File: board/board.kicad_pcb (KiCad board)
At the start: 4 copper layers, 21 x 77 mm, 72 parts, among them J1 UART, J2 008_USB, J3 DebugEdge_02x05, J4 019_100BASE-T_with_CT, J5 ADC_2x3, J6 SWD_6_Pol_Needle, J7 SPI_2x3, J8 I2C_2x2, J9 UART_2x2, U1 W25Q128JVS, U2 RP2040, U3 W5500, U4 11AA02E48, Y1 12MhZ, Y2 25MHz

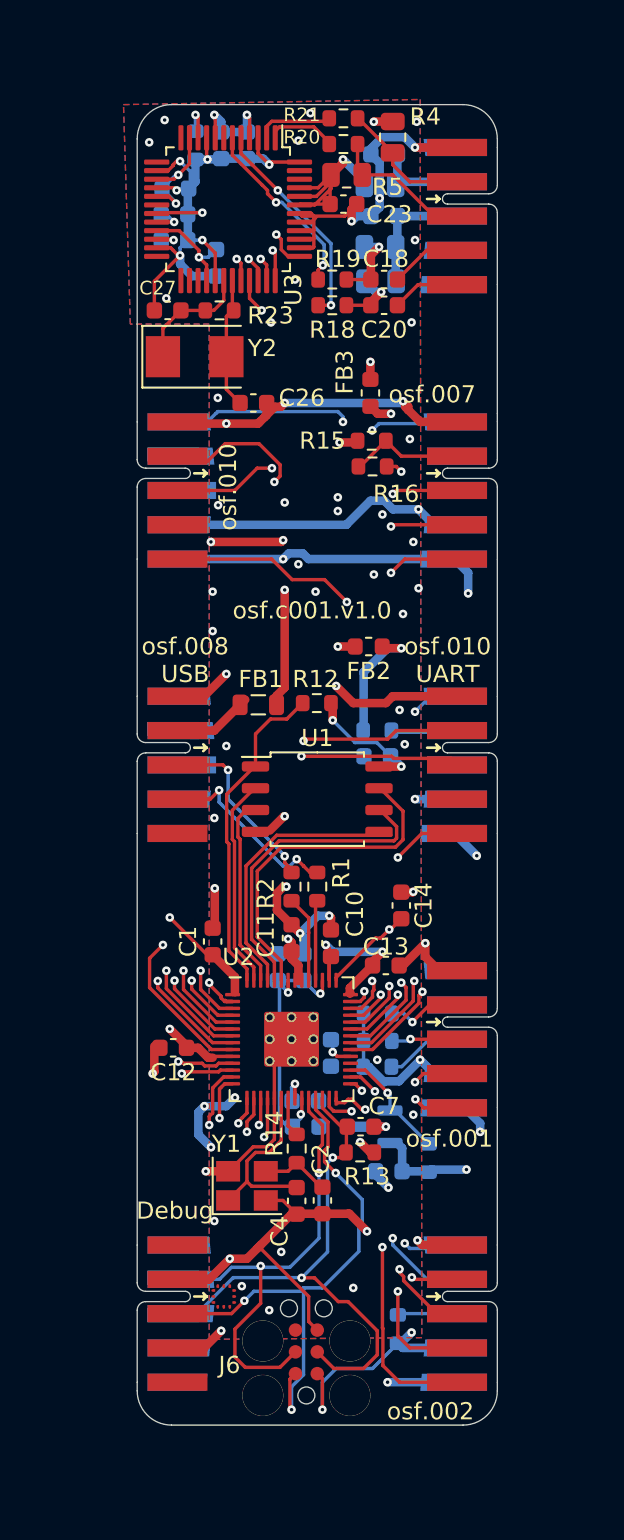
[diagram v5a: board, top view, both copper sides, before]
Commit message: updated put_on_edge connectors
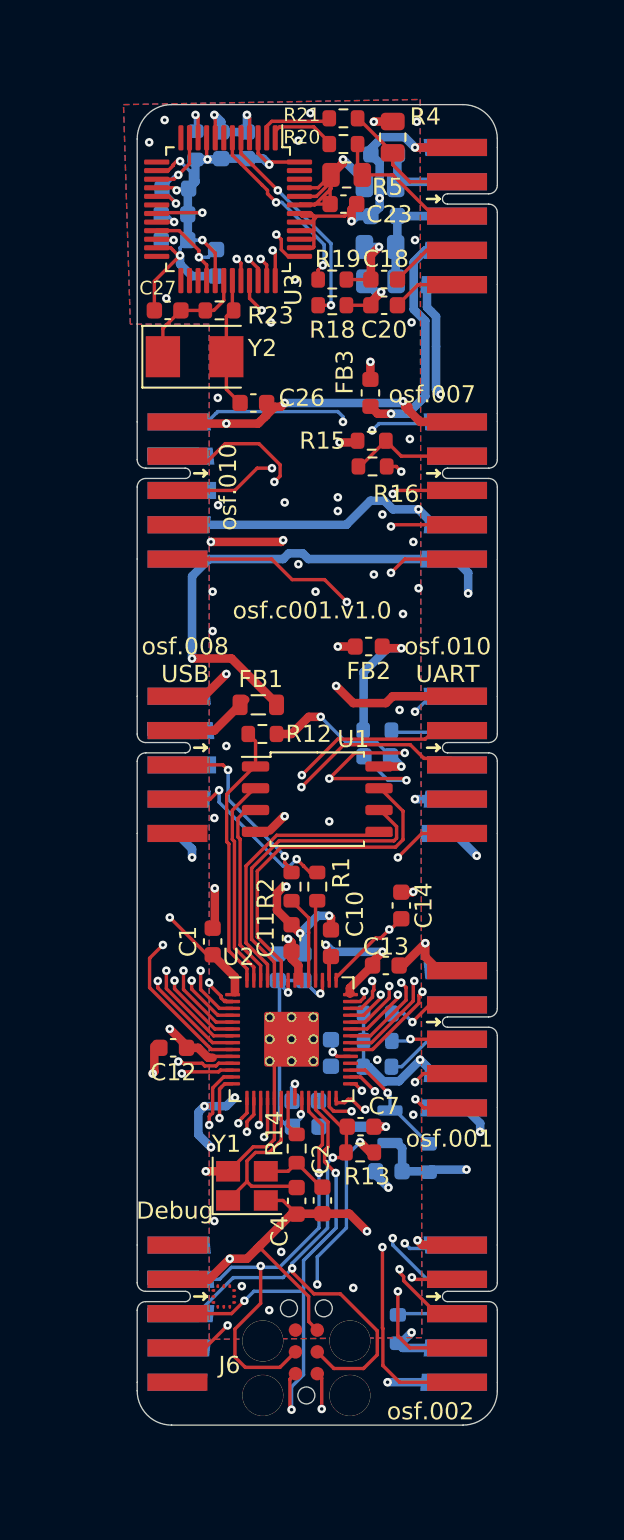
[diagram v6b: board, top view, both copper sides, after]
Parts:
- moved R12 3.65 mm to (147.3, 62.7)
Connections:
- C1 pad 1: /rp2040/VDD -> /uC3.3V
- C10 pad 1: /rp2040/VDD -> /uC3.3V
- C11 pad 1: /rp2040/VDD -> /uC3.3V
- C12 pad 1: /rp2040/VDD -> /uC3.3V
- C13 pad 1: /rp2040/VDD -> /uC3.3V
- C28 pad 1: +3V3 -> +3.3V
- C29 pad 1: /rp2040/VDD -> /uC3.3V
- C5 pad 1: /rp2040/VDD -> /uC3.3V
- C8 pad 1: /rp2040/VDD -> /uC3.3V
- FB2 pad 1: +3V3 -> +3.3V
- FB2 pad 2: /rp2040/VDD -> /uC3.3V
- FB3 pad 2: +3V3 -> +3.3V
- J1 pad 9: +3V3 -> +3.3V
- J2 pad 10: (no net) -> +5V
- J3 pad 5: +3V3 -> /uC3.3V
- J4 pad 10: (no net) -> +5V
- J4 pad 9: (no net) -> +3.3V
- J5 pad 9: +3V3 -> +3.3V
- J6 pad 1: +3V3 -> /uC3.3V
- J7 pad 9: +3V3 -> +3.3V
- J8 pad 9: +3V3 -> +3.3V
- J9 pad 9: +3V3 -> +3.3V
- R10 pad 1: +3V3 -> +3.3V
- R11 pad 1: +3V3 -> +3.3V
- R12 pad 1: /rp2040/VDD -> /uC3.3V
- R13 pad 1: /rp2040/VDD -> /uC3.3V
- R15 pad 1: /rp2040/VDD -> /uC3.3V
- R24 pad 1: +3V3 -> +3.3V
- R7 pad 1: +3V3 -> +3.3V
- R8 pad 1: +3V3 -> +3.3V
- R9 pad 1: +3V3 -> +3.3V
- U1 pad 8: /rp2040/VDD -> /uC3.3V
- U2 pad 1: /rp2040/VDD -> /uC3.3V
- U2 pad 10: /rp2040/VDD -> /uC3.3V
- U2 pad 22: /rp2040/VDD -> /uC3.3V
- U2 pad 33: /rp2040/VDD -> /uC3.3V
- U2 pad 42: /rp2040/VDD -> /uC3.3V
- U2 pad 44: /rp2040/VDD -> /uC3.3V
- U2 pad 48: /rp2040/VDD -> /uC3.3V
- U2 pad 49: /rp2040/VDD -> /uC3.3V
- U4 pad 2: +3V3 -> +3.3V
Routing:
- net /uC3.3V: track 0.00 -> 171.3 mm, vias 0 -> 17
- net /rp2040/VDD: track 139.5 -> 0.00 mm, vias 14 -> 0
- net +3V3: track 136.2 -> 0.00 mm, vias 9 -> 0
- net +3.3V: track 0.00 -> 124.9 mm, vias 0 -> 7
- net +5V: track 88.4 -> 127.8 mm, vias 6 -> 7
- net GND: track 288.4 -> 303.0 mm, vias 68 -> 71
- net /rp2040/QPI_SS: track 19.1 -> 15.8 mm
- net /rp2040/SWD: track 32.1 -> 30.1 mm
- net /UART1_TX: track 34.3 -> 33.1 mm
- added copper zone on In1.Cu, net /uC3.3V
- removed copper zone on In1.Cu, net /rp2040/VDD

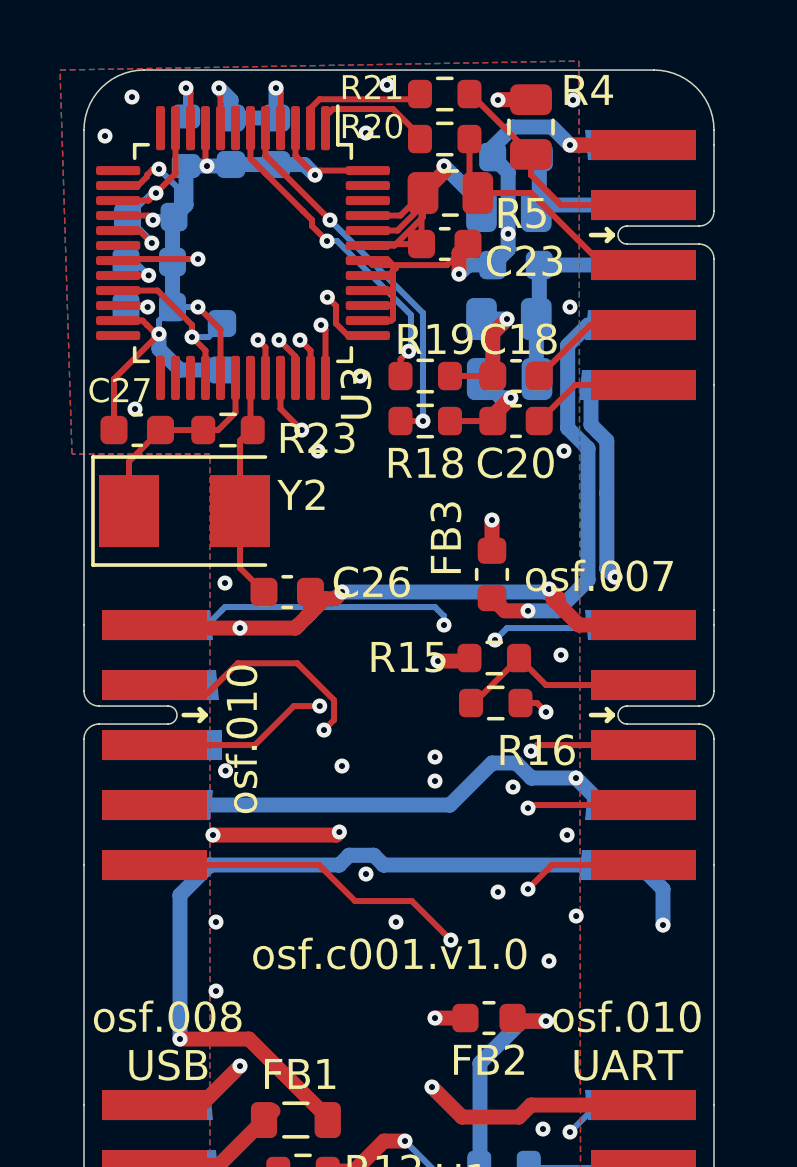
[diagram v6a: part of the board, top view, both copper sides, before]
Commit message: updated to use v1.1 of b078 to work with shorted center tap magjacks
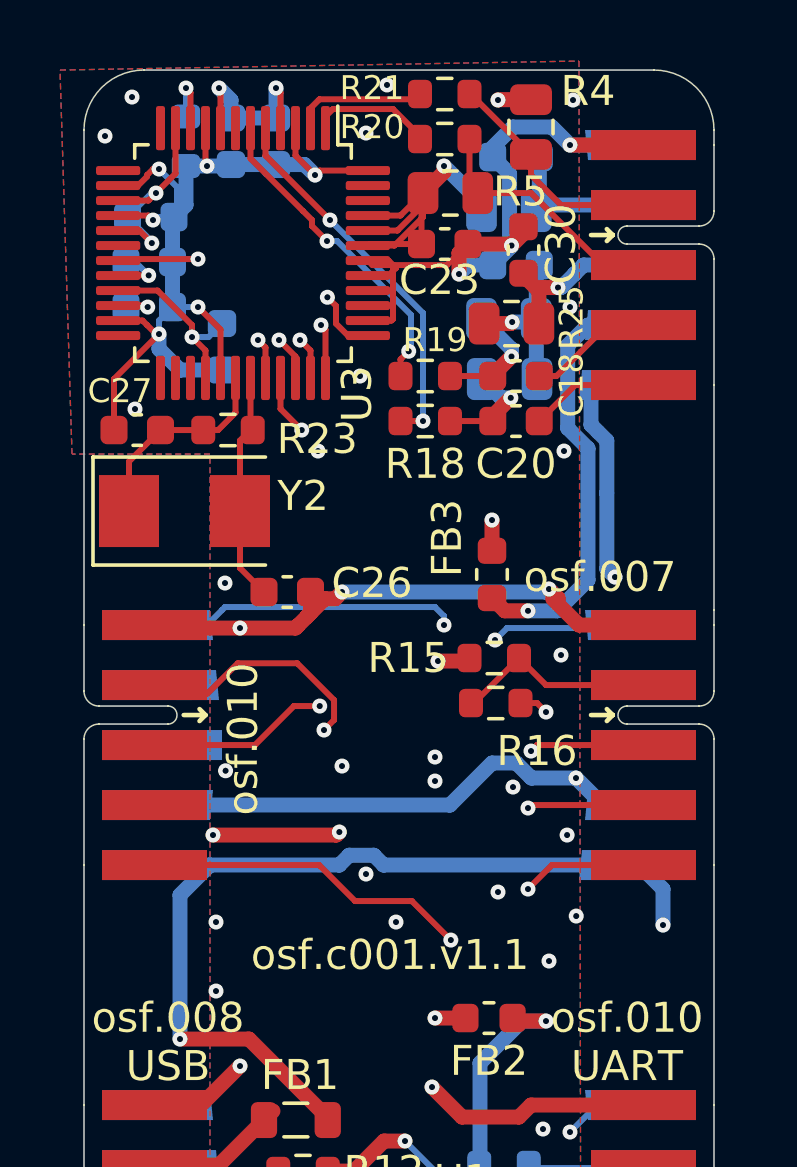
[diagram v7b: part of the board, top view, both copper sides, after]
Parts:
- added C30: 100nF, Capacitor_SMD:C_0603_1608Metric, F.Cu at (154.7, 32.0)
- added R25: d.n.p, Resistor_SMD:R_0805_2012Metric, F.Cu at (154.2, 34.5)
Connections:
- C22 pad 1: /controller/CT2 -> Net-(C22-Pad1)
- R17 pad 1: /controller/CT2 -> Net-(C22-Pad1)
- R6 pad 1: /controller/CT2 -> Net-(C22-Pad1)
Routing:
- net Net-(C22-Pad1): track 0.00 -> 5.65 mm, vias 0 -> 1
- net GND: track 303.0 -> 305.7 mm
- net /controller/CT2: track 7.33 -> 5.73 mm, vias 0 -> 1
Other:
- board text added: "osf.c001.v1.1"
- board text removed: "osf.c001.v1.0"

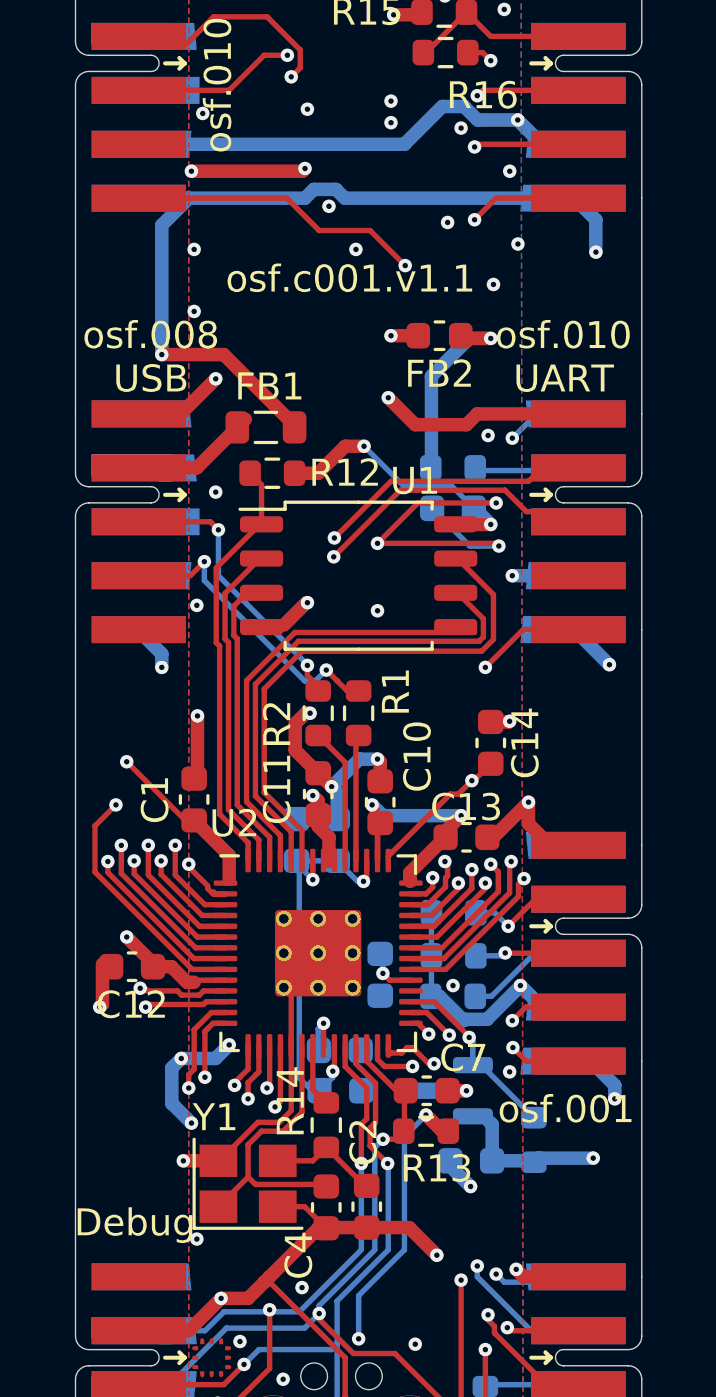
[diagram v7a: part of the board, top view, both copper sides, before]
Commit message: added boot select button and standard (small) flash
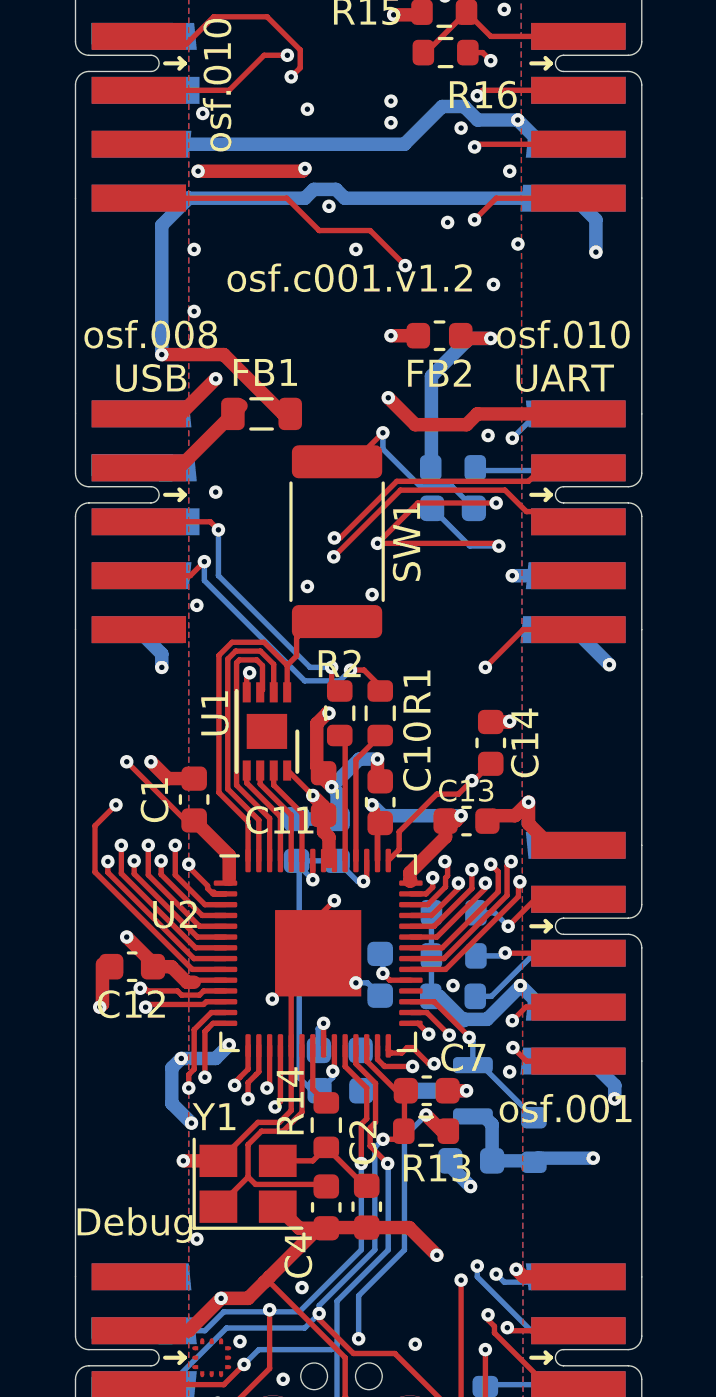
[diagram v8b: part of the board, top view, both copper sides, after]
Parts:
- removed R12: d.n.p, Resistor_SMD:R_0603_1608Metric
- added SW1: PTS636 SK25J SMTR LFS, Resistor_SMD:R_2512_6332Metric, F.Cu at (149.7, 65.2)
- U1: value W25Q128JVS -> W25Q16JVUXIQ; footprint Package_SO:SOIC-8_5.23x5.23mm_P1.27mm -> Package_DFN_QFN:DFN-8-1EP_3x2mm_P0.5mm_EP1.3x1.5mm
- U2: footprint b018:RP2040-QFN-56 -> Package_DFN_QFN:QFN-56-1EP_7x7mm_P0.4mm_EP3.2x3.2mm
- moved U1 6.70 mm to (147.1, 72.3), turned to -90 degrees
- moved R1 0.80 mm to (151.3, 71.6)
- moved R2 0.80 mm to (149.8, 71.6)
- moved C13 0.60 mm to (154.5, 75.6)
- moved FB1 0.53 mm to (146.9, 60.5)
- moved C11 0.20 mm to (149.2, 74.6)
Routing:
- net Net-(U1-IO3): track 19.8 -> 3.77 mm
- net /rp2040/QSPI_CLK: track 18.4 -> 3.81 mm
- net Net-(U1-DI(IO0)): track 16.4 -> 3.86 mm
- net GND: track 305.7 -> 315.8 mm, vias 71 -> 75
- net /uC3.3V: track 171.3 -> 169.6 mm, vias 17 -> 16
- net Net-(U1-DO(IO1)): track 12.3 -> 11.0 mm
- net Net-(U1-IO2): track 11.2 -> 9.96 mm
- net Net-(J2-DM): track 11.1 -> 12.0 mm
- net Net-(J2-DP): track 10.6 -> 11.4 mm
- net /rp2040/QPI_SS: track 15.8 -> 15.1 mm
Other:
- board text added: "osf.c001.v1.2"
- board text removed: "osf.c001.v1.1"
